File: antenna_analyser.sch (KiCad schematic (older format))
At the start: 22 parts, among them IC1 MCP6002, IC2 ARDUINO_PRO_MINI_5V, J1 SIL10, J2 SIL10

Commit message: Updated element references and their values.
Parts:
- removed R8: R, symbol R
- added C6: 10n, symbol C_Small
- added R11, R7: 648, symbol R
- C1: value CP -> 1uF
- C2: renamed from C5; value C_Small -> 100n
- C3: renamed from C4; value C_Small -> 10n
- C4: renamed from C3; value C_Small -> 100n
- C5C2: renamed from C2; value C_Small -> 10n
- D1, D2: value D -> AA143
- R1: renamed from R4; value R -> 50
- R10: renamed from R6; value R -> 10k
- R2: renamed from R1; value R -> 50
- R3: renamed from R2; value R -> 50
- R4: renamed from R7; value R -> 10k
- R5: renamed from R3; value R -> 100k
- R6: renamed from R10; value R -> 5k
- R9: value R -> 5k
- R9: renamed from R5; value R -> 100k
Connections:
- wire segments 86 -> 97

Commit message: Minor updates.
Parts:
- removed IC2: ARDUINO_PRO_MINI_5V, symbol ARDUINO_PRO_MINI_5V
- removed J1, J2: SIL10, symbol SIL10
- removed W1: TEST, symbol TEST
- added P1, P2: CONN_01X10, symbol CONN_01X10
- added P3: CONN_01X04, symbol CONN_01X04
- added P4: CONN_01X02, symbol CONN_01X02
- added SMA_E1: SMA_EDGE, symbol SMA_EDGE
- renumbered C5C2 to C5, R9 to R10, R10 to R8
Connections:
- wire segments 97 -> 88
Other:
- note added: "RESET\nDATA\nCLK\nUPDATE"
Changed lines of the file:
@@
 LIBS:contrib
 LIBS:valves
-LIBS:arduino
-LIBS:misc
-LIBS:ad9851
+LIBS:sma_edge
 LIBS:antenna_analyser-cache
 EELAYER 25 0
@@
 $EndDescr
 $Comp
-L MCP6002 IC1
-U 1 1 557082B3
-P 5300 3750
-F 0 "IC1" H 5600 4050 60  0000 C CNN
-F 1 "MCP6002" V 5300 3750 60  0000 C CNN
-F 2 "" H 5300 3750 60  0000 C CNN
-F 3 "" H 5300 3750 60  0000 C CNN
-	1    5300 3750
-	0    1    1    0
-$EndComp
-$Comp
 L R R6
 U 1 1 557082EB
@@
 $EndComp
 $Comp
-L R R9
+L R R10
 U 1 1 5570831F
 P 5250 4800
-F 0 "R9" V 5330 4800 50  0000 C CNN
+F 0 "R10" V 5330 4800 50  0000 C CNN
 F 1 "5k" V 5250 4800 50  0000 C CNN
 F 2 "" V 5180 4800 30  0000 C CNN
@@
 $EndComp
 $Comp
-L TEST W1
-U 1 1 557083DB
-P 5850 1950
-F 0 "W1" H 5850 2010 40  0000 C CNN
-F 1 "TEST" H 5850 1880 40  0000 C CNN
-F 2 "" H 5850 1950 60  0000 C CNN
-F 3 "" H 5850 1950 60  0000 C CNN
-	1    5850 1950
-	0    1    1    0
-$EndComp
-$Comp
 L GND #PWR03
 U 1 1 5570842B
@@
 $EndComp
 $Comp
-L R R10
+L R R8
 U 1 1 557089C8
 P 5150 4800
-F 0 "R10" V 5230 4800 50  0000 C CNN
+F 0 "R8" V 5230 4800 50  0000 C CNN
 F 1 "10k" V 5150 4800 50  0000 C CNN
 F 2 "" V 5080 4800 30  0000 C CNN
@@
 $EndComp
 $Comp
-L C_Small C5C2
+L C_Small C5
 U 1 1 55708AE0
 P 4900 4500
-F 0 "C5C2" H 4910 4570 50  0000 L CNN
+F 0 "C5" H 4910 4570 50  0000 L CNN
 F 1 "10n" H 4910 4420 50  0000 L CNN
 F 2 "" H 4900 4500 60  0000 C CNN
@@
 F 3 "" H 4900 3550 60  0000 C CNN
 	1    4900 3550
-	1    0    0    -1
-$EndComp
-$Comp
-L ARDUINO_PRO_MINI_5V IC2
-U 1 1 55708DE4
-P 7600 3800
-F 0 "IC2" H 8050 4600 60  0000 C CNN
-F 1 "ARDUINO_PRO_MINI_5V" V 7600 3950 60  0000 C CNN
-F 2 "" H 7600 3800 60  0000 C CNN
-F 3 "" H 7600 3800 60  0000 C CNN
-	1    7600 3800
-	1    0    0    -1
-$EndComp
-$Comp
-L GND #PWR010
-U 1 1 55708FBA
-P 8600 4200
-F 0 "#PWR010" H 8600 3950 50  0001 C CNN
-F 1 "GND" H 8600 4050 50  0000 C CNN
-F 2 "" H 8600 4200 60  0000 C CNN
-F 3 "" H 8600 4200 60  0000 C CNN
-	1    8600 4200
-	1    0    0    -1
-$EndComp
-$Comp
-L +5V #PWR011
-U 1 1 55708FE1
-P 6600 4000
-F 0 "#PWR011" H 6600 3850 50  0001 C CNN
-F 1 "+5V" H 6600 4140 50  0000 C CNN
-F 2 "" H 6600 4000 60  0000 C CNN
-F 3 "" H 6600 4000 60  0000 C CNN
-	1    6600 4000
-	1    0    0    -1
-$EndComp
-$Comp
-L SIL10 J1
-U 1 1 557092CC
-P 1300 3600
-F 0 "J1" H 1300 4200 70  0000 C CNN
-F 1 "SIL10" V 1320 3600 70  0000 C CNN
-F 2 "" H 1300 3600 60  0000 C CNN
-F 3 "" H 1300 3600 60  0000 C CNN
-	1    1300 3600
-	1    0    0    -1
-$EndComp
-$Comp
-L SIL10 J2
-U 1 1 55709389
-P 2150 3600
-F 0 "J2" H 2150 4200 70  0000 C CNN
-F 1 "SIL10" V 2170 3600 70  0000 C CNN
-F 2 "" H 2150 3600 60  0000 C CNN
-F 3 "" H 2150 3600 60  0000 C CNN
-	1    2150 3600
 	1    0    0    -1
 $EndComp
@@
 $EndComp
 $Comp
-L GND #PWR012
+L GND #PWR010
 U 1 1 55709504
 P 1550 3800
-F 0 "#PWR012" H 1550 3550 50  0001 C CNN
+F 0 "#PWR010" H 1550 3550 50  0001 C CNN
 F 1 "GND" H 1550 3650 50  0000 C CNN
 F 2 "" H 1550 3800 60  0000 C CNN
@@
 $EndComp
 $Comp
-L +5V #PWR013
+L +5V #PWR011
 U 1 1 5570988D
 P 650 3950
-F 0 "#PWR013" H 650 3800 50  0001 C CNN
+F 0 "#PWR011" H 650 3800 50  0001 C CNN
 F 1 "+5V" H 650 4090 50  0000 C CNN
 F 2 "" H 650 3950 60  0000 C CNN
@@
 $EndComp
 $Comp
-L GND #PWR014
+L GND #PWR012
 U 1 1 55709A10
 P 650 3450
-F 0 "#PWR014" H 650 3200 50  0001 C CNN
+F 0 "#PWR012" H 650 3200 50  0001 C CNN
 F 1 "GND" H 650 3300 50  0000 C CNN
 F 2 "" H 650 3450 60  0000 C CNN
@@
 $EndComp
 $Comp
-L GND #PWR015
+L GND #PWR013
 U 1 1 55717CB8
 P 5650 1950
-F 0 "#PWR015" H 5650 1700 50  0001 C CNN
+F 0 "#PWR013" H 5650 1700 50  0001 C CNN
 F 1 "GND" H 5650 1800 50  0000 C CNN
 F 2 "" H 5650 1950 60  0000 C CNN
@@
 	5450 4400 5450 4600
 Wire Wire Line
-	5850 2150 5850 2400
+	5850 2000 5850 2400
 Wire Wire Line
 	5250 2250 5250 3100
@@
 	5100 1400 5850 1400
 Wire Wire Line
-	5850 1400 5850 1750
+	5850 1400 5850 1900
 Wire Wire Line
 	5250 1400 5250 1550
@@
 Connection ~ 5100 2900
 Wire Wire Line
-	6750 3700 5850 3700
-Wire Wire Line
 	5850 3700 5850 2800
 Wire Wire Line
@@
 Connection ~ 5450 2800
 Wire Wire Line
-	5850 3800 6750 3800
-Wire Wire Line
 	5850 5200 5850 3800
 Connection ~ 5350 5200
 Wire Wire Line
-	6750 4100 6600 4100
-Wire Wire Line
-	6600 4100 6600 4000
-Wire Wire Line
-	8400 4100 8600 4100
-Wire Wire Line
-	8600 4100 8600 4200
-Wire Wire Line
 	2650 2750 3100 2750
 Wire Wire Line
@@
 	1700 2750 1700 3250
 Wire Wire Line
-	1700 3250 1800 3250
-Wire Wire Line
-	1800 3550 1550 3550
+	1700 3250 1950 3250
+Wire Wire Line
+	1550 3550 1950 3550
 Wire Wire Line
 	1550 3550 1550 3800
 Wire Wire Line
-	6750 3500 6500 3500
-Wire Wire Line
-	6500 3500 6500 6800
-Wire Wire Line
-	6500 6800 1700 6800
-Wire Wire Line
-	1700 6800 1700 3650
-Wire Wire Line
-	1700 3650 1800 3650
-Wire Wire Line
-	6750 3300 6450 3300
-Wire Wire Line
-	6450 3300 6450 6750
-Wire Wire Line
-	6450 6750 1750 6750
-Wire Wire Line
-	1750 6750 1750 3750
-Wire Wire Line
-	1750 3750 1800 3750
-Wire Wire Line
-	1800 3850 1650 3850
-Wire Wire Line
-	1650 3850 1650 6700
-Wire Wire Line
-	1650 6700 6400 6700
-Wire Wire Line
-	6400 6700 6400 3100
-Wire Wire Line
-	6400 3100 6750 3100
-Wire Wire Line
-	6750 3200 6350 3200
-Wire Wire Line
-	6350 3200 6350 6650
-Wire Wire Line
-	6350 6650 1800 6650
-Wire Wire Line
-	1800 6650 1800 3950
-Wire Wire Line
-	950  3950 650  3950
-Wire Wire Line
-	950  3850 850  3850
+	650  3950 1050 3950
+Wire Wire Line
+	850  3850 1050 3850
 Wire Wire Line
 	850  3850 850  4050
 Connection ~ 850  3950
 Wire Wire Line
-	850  4050 950  4050
-Wire Wire Line
-	950  3150 650  3150
+	850  4050 1050 4050
+Wire Wire Line
+	650  3150 1050 3150
 Wire Wire Line
 	650  3150 650  3450
 Wire Wire Line
-	950  3750 850  3750
+	850  3750 1050 3750
 Wire Wire Line
 	850  3750 850  3150
@@
 $EndComp
 $Comp
-L GND #PWR016
+L GND #PWR014
 U 1 1 557187FE
 P 6050 5050
-F 0 "#PWR016" H 6050 4800 50  0001 C CNN
+F 0 "#PWR014" H 6050 4800 50  0001 C CNN
 F 1 "GND" H 6050 4900 50  0000 C CNN
 F 2 "" H 6050 5050 60  0000 C CNN
@@
 $EndComp
 $Comp
-L GND #PWR017
+L GND #PWR015
 U 1 1 55718CAB
 P 5650 5800
-F 0 "#PWR017" H 5650 5550 50  0001 C CNN
+F 0 "#PWR015" H 5650 5550 50  0001 C CNN
 F 1 "GND" H 5650 5650 50  0000 C CNN
 F 2 "" H 5650 5800 60  0000 C CNN
@@
 	5650 4450 5650 5400
 Connection ~ 5450 4450
+$Comp
+L CONN_01X10 P1
+U 1 1 5571FE39
+P 1250 3600
+F 0 "P1" H 1250 4150 50  0000 C CNN
+F 1 "CONN_01X10" V 1350 3600 50  0000 C CNN
+F 2 "" H 1250 3600 60  0000 C CNN
+F 3 "" H 1250 3600 60  0000 C CNN
+	1    1250 3600
+	1    0    0    -1
+$EndComp
+$Comp
+L CONN_01X10 P2
+U 1 1 5571FE77
+P 2150 3600
+F 0 "P2" H 2150 4150 50  0000 C CNN
+F 1 "CONN_01X10" V 2250 3600 50  0000 C CNN
+F 2 "" H 2150 3600 60  0000 C CNN
+F 3 "" H 2150 3600 60  0000 C CNN
+	1    2150 3600
+	1    0    0    -1
+$EndComp
+$Comp
+L CONN_01X04 P3
+U 1 1 55720267
+P 2150 4600
+F 0 "P3" H 2150 4850 50  0000 C CNN
+F 1 "CONN_01X04" V 2250 4600 50  0000 C CNN
+F 2 "" H 2150 4600 60  0000 C CNN
+F 3 "" H 2150 4600 60  0000 C CNN
+	1    2150 4600
+	1    0    0    -1
+$EndComp
+Wire Wire Line
+	1950 3650 1850 3650
+Wire Wire Line
+	1850 3650 1850 4450
+Wire Wire Line
+	1850 4450 1950 4450
+Wire Wire Line
+	1950 3750 1800 3750
+Wire Wire Line
+	1800 3750 1800 4550
+Wire Wire Line
+	1800 4550 1950 4550
+Wire Wire Line
+	1950 3850 1750 3850
+Wire Wire Line
+	1750 3850 1750 4650
+Wire Wire Line
+	1750 4650 1950 4650
+Wire Wire Line
+	1950 3950 1700 3950
+Wire Wire Line
+	1700 3950 1700 4750
+Wire Wire Line
+	1700 4750 1950 4750
+Text Notes 2350 4750 0    60   ~ 0
+RESET\nDATA\nCLK\nUPDATE
+$Comp
+L CONN_01X02 P4
+U 1 1 55720A97
+P 6250 3750
+F 0 "P4" H 6250 3900 50  0000 C CNN
+F 1 "CONN_01X02" V 6350 3750 50  0000 C CNN
+F 2 "" H 6250 3750 60  0000 C CNN
+F 3 "" H 6250 3750 60  0000 C CNN
+	1    6250 3750
+	1    0    0    -1
+$EndComp
+Wire Wire Line
+	5850 3700 6050 3700
+Wire Wire Line
+	5850 3800 6050 3800
+$Comp
+L SMA_EDGE SMA_E1
+U 1 1 55720D67
+P 6300 1900
+F 0 "SMA_E1" H 6450 2200 60  0000 C CNN
+F 1 "SMA_EDGE" H 6450 2100 60  0000 C CNN
+F 2 "" H 6300 1900 60  0000 C CNN
+F 3 "" H 6300 1900 60  0000 C CNN
+	1    6300 1900
+	1    0    0    -1
+$EndComp
+Wire Wire Line
+	5850 1900 5950 1900
+Wire Wire Line
+	5950 2000 5850 2000
+$Comp
+L MCP6002 IC1
+U 1 1 55720929
+P 5300 3750
+F 0 "IC1" H 5600 4050 60  0000 C CNN
+F 1 "MCP6002" V 5300 3750 60  0000 C CNN
+F 2 "" H 5300 3750 60  0000 C CNN
+F 3 "" H 5300 3750 60  0000 C CNN
+	1    5300 3750
+	0    1    1    0
+$EndComp
 $EndSCHEMATC

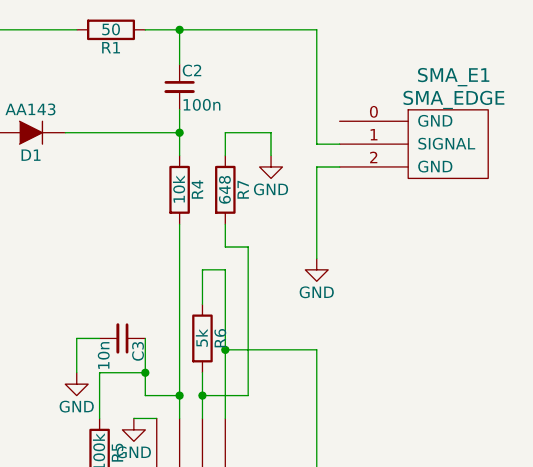
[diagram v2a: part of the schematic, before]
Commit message: Updated library references.
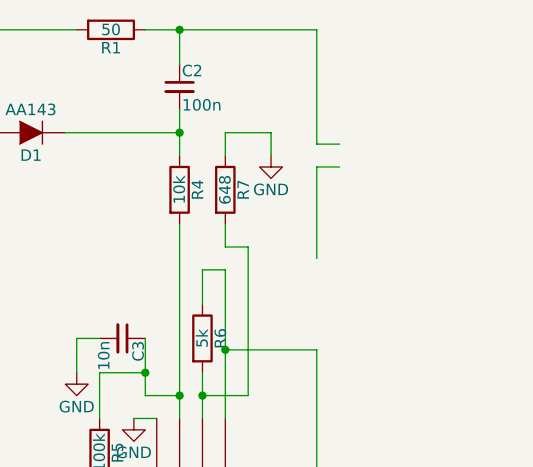
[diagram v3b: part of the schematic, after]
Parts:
- removed SMA_E1: SMA_EDGE, symbol SMA_EDGE
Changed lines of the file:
@@
 LIBS:contrib
 LIBS:valves
-LIBS:sma_edge
-LIBS:antenna_analyser-cache
+LIBS:arduino
+LIBS:misc
 EELAYER 25 0
 EELAYER END
@@
 $EndComp
 $Comp
-L GND #PWR03
-U 1 1 5570842B
-P 5850 2400
-F 0 "#PWR03" H 5850 2150 50  0001 C CNN
-F 1 "GND" H 5850 2250 50  0000 C CNN
-F 2 "" H 5850 2400 60  0000 C CNN
-F 3 "" H 5850 2400 60  0000 C CNN
-	1    5850 2400
-	1    0    0    -1
-$EndComp
-$Comp
 L R R4
 U 1 1 557084F2
@@
 Wire Wire Line
 	5850 3800 6050 3800
-$Comp
-L SMA_EDGE SMA_E1
-U 1 1 55720D67
-P 6300 1900
-F 0 "SMA_E1" H 6450 2200 60  0000 C CNN
-F 1 "SMA_EDGE" H 6450 2100 60  0000 C CNN
-F 2 "" H 6300 1900 60  0000 C CNN
-F 3 "" H 6300 1900 60  0000 C CNN
-	1    6300 1900
-	1    0    0    -1
-$EndComp
 Wire Wire Line
 	5850 1900 5950 1900

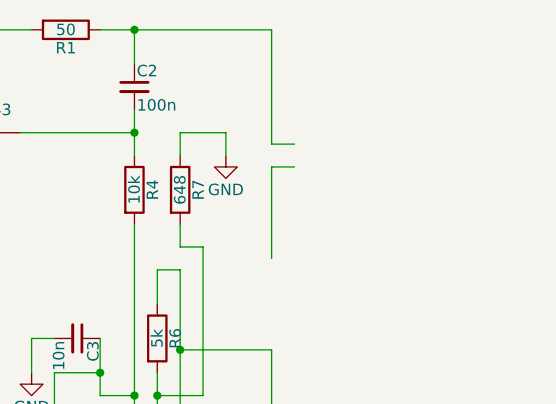
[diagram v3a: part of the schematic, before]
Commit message: The antenna connector is an SMA edge connector now.
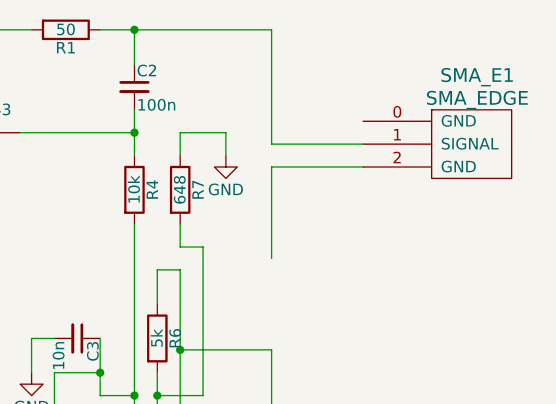
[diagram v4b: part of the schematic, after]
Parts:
- added SMA_E1: SMA_EDGE, symbol SMA_EDGE
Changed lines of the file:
@@
 LIBS:arduino
 LIBS:misc
+LIBS:sma_edge
+LIBS:antenna_analyser-cache
 EELAYER 25 0
 EELAYER END
@@
 $EndComp
 $Comp
-L GND #PWR04
+L GND #PWR03
 U 1 1 55708577
 P 4800 2900
-F 0 "#PWR04" H 4800 2650 50  0001 C CNN
+F 0 "#PWR03" H 4800 2650 50  0001 C CNN
 F 1 "GND" H 4800 2750 50  0000 C CNN
 F 2 "" H 4800 2900 60  0000 C CNN
@@
 $EndComp
 $Comp
-L GND #PWR05
+L GND #PWR04
 U 1 1 557088AE
 P 4050 2550
-F 0 "#PWR05" H 4050 2300 50  0001 C CNN
+F 0 "#PWR04" H 4050 2300 50  0001 C CNN
 F 1 "GND" H 4050 2400 50  0000 C CNN
 F 2 "" H 4050 2550 60  0000 C CNN
@@
 $EndComp
 $Comp
-L GND #PWR06
+L GND #PWR05
 U 1 1 5570893A
 P 4900 6250
-F 0 "#PWR06" H 4900 6000 50  0001 C CNN
+F 0 "#PWR05" H 4900 6000 50  0001 C CNN
 F 1 "GND" H 4900 6100 50  0000 C CNN
 F 2 "" H 4900 6250 60  0000 C CNN
@@
 $EndComp
 $Comp
-L GND #PWR07
+L GND #PWR06
 U 1 1 55708B2C
 P 4700 4650
-F 0 "#PWR07" H 4700 4400 50  0001 C CNN
+F 0 "#PWR06" H 4700 4400 50  0001 C CNN
 F 1 "GND" H 4700 4500 50  0000 C CNN
 F 2 "" H 4700 4650 60  0000 C CNN
@@
 $EndComp
 $Comp
-L GND #PWR08
+L GND #PWR07
 U 1 1 55708C34
 P 4950 5250
-F 0 "#PWR08" H 4950 5000 50  0001 C CNN
+F 0 "#PWR07" H 4950 5000 50  0001 C CNN
 F 1 "GND" H 4950 5100 50  0000 C CNN
 F 2 "" H 4950 5250 60  0000 C CNN
@@
 $EndComp
 $Comp
-L GND #PWR09
+L GND #PWR08
 U 1 1 55708C5A
 P 4900 3550
-F 0 "#PWR09" H 4900 3300 50  0001 C CNN
+F 0 "#PWR08" H 4900 3300 50  0001 C CNN
 F 1 "GND" H 4900 3400 50  0000 C CNN
 F 2 "" H 4900 3550 60  0000 C CNN
@@
 $EndComp
 $Comp
-L GND #PWR010
+L GND #PWR09
 U 1 1 55709504
 P 1550 3800
-F 0 "#PWR010" H 1550 3550 50  0001 C CNN
+F 0 "#PWR09" H 1550 3550 50  0001 C CNN
 F 1 "GND" H 1550 3650 50  0000 C CNN
 F 2 "" H 1550 3800 60  0000 C CNN
@@
 $EndComp
 $Comp
-L +5V #PWR011
+L +5V #PWR010
 U 1 1 5570988D
 P 650 3950
-F 0 "#PWR011" H 650 3800 50  0001 C CNN
+F 0 "#PWR010" H 650 3800 50  0001 C CNN
 F 1 "+5V" H 650 4090 50  0000 C CNN
 F 2 "" H 650 3950 60  0000 C CNN
@@
 $EndComp
 $Comp
-L GND #PWR012
+L GND #PWR011
 U 1 1 55709A10
 P 650 3450
-F 0 "#PWR012" H 650 3200 50  0001 C CNN
+F 0 "#PWR011" H 650 3200 50  0001 C CNN
 F 1 "GND" H 650 3300 50  0000 C CNN
 F 2 "" H 650 3450 60  0000 C CNN
@@
 $EndComp
 $Comp
-L GND #PWR013
+L GND #PWR012
 U 1 1 55717CB8
 P 5650 1950
-F 0 "#PWR013" H 5650 1700 50  0001 C CNN
+F 0 "#PWR012" H 5650 1700 50  0001 C CNN
 F 1 "GND" H 5650 1800 50  0000 C CNN
 F 2 "" H 5650 1950 60  0000 C CNN
@@
 $EndComp
 $Comp
-L GND #PWR014
+L GND #PWR013
 U 1 1 557187FE
 P 6050 5050
-F 0 "#PWR014" H 6050 4800 50  0001 C CNN
+F 0 "#PWR013" H 6050 4800 50  0001 C CNN
 F 1 "GND" H 6050 4900 50  0000 C CNN
 F 2 "" H 6050 5050 60  0000 C CNN
@@
 $EndComp
 $Comp
-L GND #PWR015
+L GND #PWR014
 U 1 1 55718CAB
 P 5650 5800
-F 0 "#PWR015" H 5650 5550 50  0001 C CNN
+F 0 "#PWR014" H 5650 5550 50  0001 C CNN
 F 1 "GND" H 5650 5650 50  0000 C CNN
 F 2 "" H 5650 5800 60  0000 C CNN
@@
 	5850 3800 6050 3800
 Wire Wire Line
-	5850 1900 5950 1900
-Wire Wire Line
-	5950 2000 5850 2000
+	5850 1900 6250 1900
+Wire Wire Line
+	5850 2000 6250 2000
 $Comp
 L MCP6002 IC1
@@
 	0    1    1    0
 $EndComp
+$Comp
+L SMA_EDGE SMA_E1
+U 1 1 558B1D24
+P 6600 1900
+F 0 "SMA_E1" H 6750 2200 60  0000 C CNN
+F 1 "SMA_EDGE" H 6750 2100 60  0000 C CNN
+F 2 "" H 6600 1900 60  0000 C CNN
+F 3 "" H 6600 1900 60  0000 C CNN
+	1    6600 1900
+	1    0    0    -1
+$EndComp
 $EndSCHEMATC

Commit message: ???
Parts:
- C1: footprint (none) -> Capacitors_Elko_ThroughHole:Elko_vert_20x10mm_RM2.5
- C2, C3, C4, C5, C6: footprint (none) -> Capacitors_ThroughHole:C_Disc_D3_P2.5
- D1, D2: footprint (none) -> Diodes_ThroughHole:Diode_DO-41_SOD81_Horizontal_RM10
- IC1: footprint (none) -> sop8:SOP-8
- P1, P2: footprint (none) -> Pin_Headers:Pin_Header_Straight_1x10
- P3: footprint (none) -> Pin_Headers:Pin_Header_Straight_1x04
- P4: footprint (none) -> Pin_Headers:Pin_Header_Straight_1x02
- R1, R10, R11, R2, R3, R4, R5, R6, R7, R8, R9: footprint (none) -> Resistors_ThroughHole:Resistor_Horizontal_RM10mm
- SMA_E1: footprint (none) -> SMA_EDGE:SMA_EDGE
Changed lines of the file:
@@
 F 0 "R6" V 5430 2750 50  0000 C CNN
 F 1 "5k" V 5350 2750 50  0000 C CNN
-F 2 "" V 5280 2750 30  0000 C CNN
+F 2 "Resistors_ThroughHole:Resistor_Horizontal_RM10mm" V 5280 2750 30  0001 C CNN
 F 3 "" H 5350 2750 30  0000 C CNN
 	1    5350 2750
@@
 F 0 "R10" V 5330 4800 50  0000 C CNN
 F 1 "5k" V 5250 4800 50  0000 C CNN
-F 2 "" V 5180 4800 30  0000 C CNN
+F 2 "Resistors_ThroughHole:Resistor_Horizontal_RM10mm" V 5180 4800 30  0001 C CNN
 F 3 "" H 5250 4800 30  0000 C CNN
 	1    5250 4800
@@
 F 0 "R4" V 5330 2100 50  0000 C CNN
 F 1 "10k" V 5250 2100 50  0000 C CNN
-F 2 "" V 5180 2100 30  0000 C CNN
+F 2 "Resistors_ThroughHole:Resistor_Horizontal_RM10mm" V 5180 2100 30  0001 C CNN
 F 3 "" H 5250 2100 30  0000 C CNN
 	1    5250 2100
@@
 F 0 "C3" H 5010 2820 50  0000 L CNN
 F 1 "10n" H 5010 2670 50  0000 L CNN
-F 2 "" H 5000 2750 60  0000 C CNN
+F 2 "Capacitors_ThroughHole:C_Disc_D3_P2.5" H 5000 2750 60  0001 C CNN
 F 3 "" H 5000 2750 60  0000 C CNN
 	1    5000 2750
@@
 F 0 "D1" H 4600 1950 50  0000 C CNN
 F 1 "AA143" H 4600 1750 50  0000 C CNN
-F 2 "" H 4600 1850 60  0000 C CNN
+F 2 "Diodes_ThroughHole:Diode_DO-41_SOD81_Horizontal_RM10" H 4600 1850 60  0001 C CNN
 F 3 "" H 4600 1850 60  0000 C CNN
 	1    4600 1850
@@
 F 0 "D2" H 4600 5650 50  0000 C CNN
 F 1 "AA143" H 4600 5450 50  0000 C CNN
-F 2 "" H 4600 5550 60  0000 C CNN
+F 2 "Diodes_ThroughHole:Diode_DO-41_SOD81_Horizontal_RM10" H 4600 5550 60  0001 C CNN
 F 3 "" H 4600 5550 60  0000 C CNN
 	1    4600 5550
@@
 F 0 "C2" H 5260 1720 50  0000 L CNN
 F 1 "100n" H 5260 1570 50  0000 L CNN
-F 2 "" H 5250 1650 60  0000 C CNN
+F 2 "Capacitors_ThroughHole:C_Disc_D3_P2.5" H 5250 1650 60  0001 C CNN
 F 3 "" H 5250 1650 60  0000 C CNN
 	1    5250 1650
@@
 F 0 "R1" V 5030 1400 50  0000 C CNN
 F 1 "50" V 4950 1400 50  0000 C CNN
-F 2 "" V 4880 1400 30  0000 C CNN
+F 2 "Resistors_ThroughHole:Resistor_Horizontal_RM10mm" V 4880 1400 30  0001 C CNN
 F 3 "" H 4950 1400 30  0000 C CNN
 	1    4950 1400
@@
 F 0 "R2" V 4130 1600 50  0000 C CNN
 F 1 "50" V 4050 1600 50  0000 C CNN
-F 2 "" V 3980 1600 30  0000 C CNN
+F 2 "Resistors_ThroughHole:Resistor_Horizontal_RM10mm" V 3980 1600 30  0001 C CNN
 F 3 "" H 4050 1600 30  0000 C CNN
 	1    4050 1600
@@
 F 0 "R3" V 4130 2150 50  0000 C CNN
 F 1 "50" V 4050 2150 50  0000 C CNN
-F 2 "" V 3980 2150 30  0000 C CNN
+F 2 "Resistors_ThroughHole:Resistor_Horizontal_RM10mm" V 3980 2150 30  0001 C CNN
 F 3 "" H 4050 2150 30  0000 C CNN
 	1    4050 2150
@@
 F 0 "C4" H 4910 5970 50  0000 L CNN
 F 1 "100n" H 4910 5820 50  0000 L CNN
-F 2 "" H 4900 5900 60  0000 C CNN
+F 2 "Capacitors_ThroughHole:C_Disc_D3_P2.5" H 4900 5900 60  0001 C CNN
 F 3 "" H 4900 5900 60  0000 C CNN
 	1    4900 5900
@@
 F 0 "R8" V 5230 4800 50  0000 C CNN
 F 1 "10k" V 5150 4800 50  0000 C CNN
-F 2 "" V 5080 4800 30  0000 C CNN
+F 2 "Resistors_ThroughHole:Resistor_Horizontal_RM10mm" V 5080 4800 30  0001 C CNN
 F 3 "" H 5150 4800 30  0000 C CNN
 	1    5150 4800
@@
 F 0 "C5" H 4910 4570 50  0000 L CNN
 F 1 "10n" H 4910 4420 50  0000 L CNN
-F 2 "" H 4900 4500 60  0000 C CNN
+F 2 "Capacitors_ThroughHole:C_Disc_D3_P2.5" H 4900 4500 60  0001 C CNN
 F 3 "" H 4900 4500 60  0000 C CNN
 	1    4900 4500
@@
 F 0 "R9" V 5030 4950 50  0000 C CNN
 F 1 "100k" V 4950 4950 50  0000 C CNN
-F 2 "" V 4880 4950 30  0000 C CNN
+F 2 "Resistors_ThroughHole:Resistor_Horizontal_RM10mm" V 4880 4950 30  0001 C CNN
 F 3 "" H 4950 4950 30  0000 C CNN
 	1    4950 4950
@@
 F 0 "R5" V 4980 3250 50  0000 C CNN
 F 1 "100k" V 4900 3250 50  0000 C CNN
-F 2 "" V 4830 3250 30  0000 C CNN
+F 2 "Resistors_ThroughHole:Resistor_Horizontal_RM10mm" V 4830 3250 30  0001 C CNN
 F 3 "" H 4900 3250 30  0000 C CNN
 	1    4900 3250
@@
 F 0 "C1" H 2525 2850 50  0000 L CNN
 F 1 "1uF" H 2525 2650 50  0000 L CNN
-F 2 "" H 2538 2600 30  0000 C CNN
+F 2 "Capacitors_Elko_ThroughHole:Elko_vert_20x10mm_RM2.5" H 2538 2600 30  0001 C CNN
 F 3 "" H 2500 2750 60  0000 C CNN
 	1    2500 2750
@@
 F 0 "R7" V 5530 2100 50  0000 C CNN
 F 1 "648" V 5450 2100 50  0000 C CNN
-F 2 "" V 5380 2100 30  0000 C CNN
+F 2 "Resistors_ThroughHole:Resistor_Horizontal_RM10mm" V 5380 2100 30  0001 C CNN
 F 3 "" H 5450 2100 30  0000 C CNN
 	1    5450 2100
@@
 F 0 "R11" V 6130 4650 50  0000 C CNN
 F 1 "648" V 6050 4650 50  0000 C CNN
-F 2 "" V 5980 4650 30  0000 C CNN
+F 2 "Resistors_ThroughHole:Resistor_Horizontal_RM10mm" V 5980 4650 30  0001 C CNN
 F 3 "" H 6050 4650 30  0000 C CNN
 	1    6050 4650
@@
 F 0 "C6" H 5660 5570 50  0000 L CNN
 F 1 "10n" H 5660 5420 50  0000 L CNN
-F 2 "" H 5650 5500 60  0000 C CNN
+F 2 "Capacitors_ThroughHole:C_Disc_D3_P2.5" H 5650 5500 60  0001 C CNN
 F 3 "" H 5650 5500 60  0000 C CNN
 	1    5650 5500
@@
 F 0 "P1" H 1250 4150 50  0000 C CNN
 F 1 "CONN_01X10" V 1350 3600 50  0000 C CNN
-F 2 "" H 1250 3600 60  0000 C CNN
+F 2 "Pin_Headers:Pin_Header_Straight_1x10" H 1250 3600 60  0001 C CNN
 F 3 "" H 1250 3600 60  0000 C CNN
 	1    1250 3600
@@
 F 0 "P2" H 2150 4150 50  0000 C CNN
 F 1 "CONN_01X10" V 2250 3600 50  0000 C CNN
-F 2 "" H 2150 3600 60  0000 C CNN
+F 2 "Pin_Headers:Pin_Header_Straight_1x10" H 2150 3600 60  0001 C CNN
 F 3 "" H 2150 3600 60  0000 C CNN
 	1    2150 3600
@@
 F 0 "P3" H 2150 4850 50  0000 C CNN
 F 1 "CONN_01X04" V 2250 4600 50  0000 C CNN
-F 2 "" H 2150 4600 60  0000 C CNN
+F 2 "Pin_Headers:Pin_Header_Straight_1x04" H 2150 4600 60  0001 C CNN
 F 3 "" H 2150 4600 60  0000 C CNN
 	1    2150 4600
@@
 F 0 "P4" H 6250 3900 50  0000 C CNN
 F 1 "CONN_01X02" V 6350 3750 50  0000 C CNN
-F 2 "" H 6250 3750 60  0000 C CNN
+F 2 "Pin_Headers:Pin_Header_Straight_1x02" H 6250 3750 60  0001 C CNN
 F 3 "" H 6250 3750 60  0000 C CNN
 	1    6250 3750
@@
 F 0 "IC1" H 5600 4050 60  0000 C CNN
 F 1 "MCP6002" V 5300 3750 60  0000 C CNN
-F 2 "" H 5300 3750 60  0000 C CNN
+F 2 "sop8:SOP-8" H 5300 3750 60  0001 C CNN
 F 3 "" H 5300 3750 60  0000 C CNN
 	1    5300 3750
@@
 F 0 "SMA_E1" H 6750 2200 60  0000 C CNN
 F 1 "SMA_EDGE" H 6750 2100 60  0000 C CNN
-F 2 "" H 6600 1900 60  0000 C CNN
+F 2 "SMA_EDGE:SMA_EDGE" H 6600 1900 60  0001 C CNN
 F 3 "" H 6600 1900 60  0000 C CNN
 	1    6600 1900
